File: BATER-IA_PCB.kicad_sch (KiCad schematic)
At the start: 21 parts, among them J1 PJ-202A, J11 Conn_01x08, J15 Conn_01x08, J17 Conn_01x08, J21 Conn_01x10, J23 Conn_01x08, J5 Conn_01x08, J8 Conn_02x18_Counter_Clockwise, U1 74LS245, U17 74LS245, U2 74LS245, U3 74LS245, U4 L7805CV, U5 LD1117V33

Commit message: BUGFIX: The Diagram error in to relay module was fixed.
The routing error in the relay diagram was fixed, also, a prototype of the relay circuit was build and the functionality was validated satisfactorily
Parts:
- removed C1: 100uF, Capacitor_THT:CP_Radial_D8.0mm_P5.00mm, symbol Device:C
- removed C2: 330nF, Capacitor_THT:C_Disc_D8.0mm_W5.0mm_P5.00mm, symbol Device:C
- removed C3, C4: 100nF, Capacitor_THT:C_Disc_D8.0mm_W5.0mm_P5.00mm, symbol Device:C
- removed C5: 10uF, Capacitor_THT:CP_Radial_D8.0mm_P5.00mm, symbol Device:C
- removed D15: 1N5819, digikey-footprints:DO-41, symbol dk_Diodes-Rectifiers-Single:1N5819
- removed F1: 2A, Fuse:Fuseholder_Clip-5x20mm_Bel_FC-203-22_Lateral_P17.80x5.00mm_D1.17mm_Horizontal, symbol Device:Fuse
- removed J1: PJ-202A, digikey-footprints:Barrel_Jack_5.5mmODx2.1mmID_PJ-202A, symbol dk_Barrel-Power-Connectors:PJ-202A
- removed J15, J17, J23, J5: Conn_01x08, Connector_PinHeader_2.54mm:PinHeader_1x08_P2.54mm_Vertical, symbol Connector_Generic:Conn_01x08
- removed J21: Conn_01x10, Connector_PinHeader_2.54mm:PinHeader_1x08_P2.54mm_Vertical, symbol Connector_Generic:Conn_01x10
- removed J8: Conn_02x18_Counter_Clockwise, Connector_PinHeader_2.54mm:PinHeader_2x18_P2.54mm_Vertical, symbol Connector_Generic:Conn_02x18_Counter_Clockwise
- removed U1, U17, U2, U3: 74LS245, Package_DIP:DIP-20_W7.62mm_LongPads, symbol 74xx:74LS245
- removed U4: L7805CV, digikey-footprints:TO-220-3, symbol dk_PMIC-Voltage-Regulators-Linear:L7805CV
- removed U5: LD1117V33, digikey-footprints:TO-220-3, symbol dk_PMIC-Voltage-Regulators-Linear:LD1117V33
- added J1: Conn_01x03, Connector_PinHeader_2.54mm:PinHeader_1x03_P2.54mm_Vertical, symbol Connector_Generic:Conn_01x03
- added J3: Conn_01x12, Connector_PinHeader_2.54mm:PinHeader_1x12_P2.54mm_Vertical, symbol Connector_Generic:Conn_01x12
- added J4: Conn_02x17_Counter_Clockwise, symbol Connector_Generic:Conn_02x17_Counter_Clockwise
- renumbered J11 to J2
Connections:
- net D22: now also J4.1 (Pin_1)
- net D23: now also J4.34 (Pin_34)
- net D24: now also J4.2 (Pin_2)
- net D25: now also J4.33 (Pin_33)
- net D26: now also J4.3 (Pin_3)
- net D27: now also J4.32 (Pin_32)
- net D28: now also J4.4 (Pin_4)
- net D29: now also J4.31 (Pin_31)
- net D30: now also J4.5 (Pin_5)
- net D31: now also J4.30 (Pin_30)
- net D32: now also J4.6 (Pin_6)
- net D33: now also J4.29 (Pin_29)
- net D34: now also J4.7 (Pin_7)
- net D35: now also J4.28 (Pin_28)
- net D36: now also J4.8 (Pin_8)
- net D37: now also J4.27 (Pin_27)
- net D38: now also J4.9 (Pin_9)
- net D39: now also J4.26 (Pin_26)
- net D40: now also J4.10 (Pin_10)
- net D41: now also J4.25 (Pin_25)
- net D42: now also J4.11 (Pin_11)
- net D43: now also J4.24 (Pin_24)
- net D44: now also J4.12 (Pin_12)
- net D45: now also J4.23 (Pin_23)
- net D46: now also J4.13 (Pin_13)
- net D47: now also J4.22 (Pin_22)
- net D48: now also J4.14 (Pin_14)
- net D49: now also J4.21 (Pin_21)
- net D50: now also J4.15 (Pin_15)
- net D51: now also J4.20 (Pin_20)
- net D52: now also J4.16 (Pin_16)
- net D53: now also J4.19 (Pin_19)
- net GND: now also J1.3 (Pin_3), J4.17 (Pin_17), J4.18 (Pin_18)
- net SCL1: now also J1.1 (Pin_1)
- net SDA1: now also J1.2 (Pin_2)
- new net PWM_02: J3.12 (Pin_12)
- new net PWM_03: J3.11 (Pin_11)
- new net PWM_04: J3.10 (Pin_10)
- new net PWM_05: J3.9 (Pin_9)
- new net PWM_06: J3.8 (Pin_8)
- new net PWM_07: J3.7 (Pin_7)
- new net PWM_08: J3.6 (Pin_6)
- new net PWM_09: J3.5 (Pin_5)
- new net PWM_10: J3.4 (Pin_4)
- new net PWM_11: J3.3 (Pin_3)
- new net PWM_12: J3.2 (Pin_2)
- new net PWM_13: J3.1 (Pin_1)
- no-connect marks 27 -> 0
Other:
- sheet RELAY MODULE renamed RELAY MODULE 1
- removed sheet BMS
- added sheet BUFFER LEVEL SHIFTER (Buffer_level_shifters.kicad_sch)
- added sheet RELAY MODULE 2 (RELAY_MODULE_1_REV1.kicad_sch)
- added sheet VOLTAGE REGULATION MODULE (Voltage_regulation_module.kicad_sch)
- sheet RELAY MODULE 1: file RELAY_MODULE_V1.kicad_sch -> RELAY_MODULE_1_REV1.kicad_sch
- sheet RELAY MODULE 1 ports: added K1_COM, K1_N_C, K1_N_O, K2_COM, K2_N_C, K2_N_O, K3_COM, K3_N_C, K3_N_O, K4_COM, K4_N_C, K4_N_O, K5_COM, K5_N_C, K5_N_O, K6_COM, K6_N_C, K6_N_O; removed K10, K11, K7, K8, K9
- note added: "Buffer enable pins"
- moved on the sheet: J2

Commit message: PCB REV 001 design
The design of the first revition of the PCB is complete.
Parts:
- added C1: 100uF, Capacitor_THT:CP_Radial_D8.0mm_P5.00mm, symbol Device:C
- added D1, D11, D13, D15, D17, D3, D5, D7, D9: 1N5817, digikey-footprints:DO-41, symbol dk_Diodes-Rectifiers-Single:1N5819
- added D10, D12, D14, D16, D2, D4, D6, D8: 3.3V, Diode_THT:D_DO-35_SOD27_P10.16mm_Horizontal, symbol Device:D_Zener
- added F1: 2A, Fuse:Fuseholder_Clip-5x20mm_Bel_FC-203-22_Lateral_P17.80x5.00mm_D1.17mm_Horizontal, symbol Device:Fuse
- added J10: PWM CH4, Connector_PinHeader_2.54mm:PinHeader_1x03_P2.54mm_Vertical, symbol Connector_Generic:Conn_01x03
- added J11: PWM CH5, Connector_PinHeader_2.54mm:PinHeader_1x03_P2.54mm_Vertical, symbol Connector_Generic:Conn_01x03
- added J12: PWM CH6, Connector_PinHeader_2.54mm:PinHeader_1x03_P2.54mm_Vertical, symbol Connector_Generic:Conn_01x03
- added J13, J14, J15: PWM GP CH1, Connector_PinHeader_2.54mm:PinHeader_1x03_P2.54mm_Vertical, symbol Connector_Generic:Conn_01x03
- added J16: STP_MOTOR_1, digikey-footprints:PinHeader_1x5_P2.5mm_Drill1.1mm, symbol dk_Rectangular-Connectors-Headers-Male-Pins:B5B-XH-A_LF__SN_
- added J17: STP_MOTOR_2, digikey-footprints:PinHeader_1x5_P2.5mm_Drill1.1mm, symbol dk_Rectangular-Connectors-Headers-Male-Pins:B5B-XH-A_LF__SN_
- added J18: STP_MOTOR_3, digikey-footprints:PinHeader_1x5_P2.5mm_Drill1.1mm, symbol dk_Rectangular-Connectors-Headers-Male-Pins:B5B-XH-A_LF__SN_
- added J19: CELL 1, digikey-footprints:PinHeader_1x2_P2.5mm_Drill1.1mm, symbol dk_Rectangular-Connectors-Headers-Male-Pins:B2B-XH-A_LF__SN_
- added J20: CELL 2, digikey-footprints:PinHeader_1x2_P2.5mm_Drill1.1mm, symbol dk_Rectangular-Connectors-Headers-Male-Pins:B2B-XH-A_LF__SN_
- added J21: CELL 3, digikey-footprints:PinHeader_1x2_P2.5mm_Drill1.1mm, symbol dk_Rectangular-Connectors-Headers-Male-Pins:B2B-XH-A_LF__SN_
- added J22: LIN ACT 1, digikey-footprints:PinHeader_1x2_P2.5mm_Drill1.1mm, symbol dk_Rectangular-Connectors-Headers-Male-Pins:B2B-XH-A_LF__SN_
- added J23: LIN ACT 2, digikey-footprints:PinHeader_1x2_P2.5mm_Drill1.1mm, symbol dk_Rectangular-Connectors-Headers-Male-Pins:B2B-XH-A_LF__SN_
- added J24: LIN ACT 3, digikey-footprints:PinHeader_1x2_P2.5mm_Drill1.1mm, symbol dk_Rectangular-Connectors-Headers-Male-Pins:B2B-XH-A_LF__SN_
- added J5: GPIOS, Connector_PinHeader_2.54mm:PinHeader_1x08_P2.54mm_Vertical, symbol Connector_Generic:Conn_01x08
- added J6: PJ-202A, digikey-footprints:Barrel_Jack_5.5mmODx2.1mmID_PJ-202A, symbol dk_Barrel-Power-Connectors:PJ-202A
- added J7: PWM CH1, Connector_PinHeader_2.54mm:PinHeader_1x03_P2.54mm_Vertical, symbol Connector_Generic:Conn_01x03
- added J8: PWM CH2, Connector_PinHeader_2.54mm:PinHeader_1x03_P2.54mm_Vertical, symbol Connector_Generic:Conn_01x03
- added J9: PWM CH3, Connector_PinHeader_2.54mm:PinHeader_1x03_P2.54mm_Vertical, symbol Connector_Generic:Conn_01x03
- added R1, R2, R3: 5.1, Resistor_THT:R_Axial_DIN0614_L14.3mm_D5.7mm_P15.24mm_Horizontal, symbol Device:R_US
- J2: renamed from J1; value Conn_01x03 -> MCU_I2C_1
- J3: value Conn_01x12 -> MCU_PWM_INPUT
- J4: value Conn_02x17_Counter_Clockwise -> MCU_GPIOS_NPUT; footprint (none) -> Connector_PinHeader_2.54mm:PinHeader_2x17_P2.54mm_Vertical
- renumbered J2 to J1
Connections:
- net +3.3V: now also D1.K, D11.K, D13.K, D15.K, D3.K, D5.K, D7.K, D9.K
- net +5V: now also J10.1 (Pin_1), J11.1 (Pin_1), J12.1 (Pin_1), J13.1 (Pin_1), J14.1 (Pin_1), J15.1 (Pin_1), J7.1 (Pin_1), J8.1 (Pin_1), J9.1 (Pin_1)
- net ADC_CH0: now also D1.A, D2.1 (K)
- net ADC_CH1: now also D3.A, D4.1 (K)
- net ADC_CH2: now also D5.A, D6.1 (K)
- net ADC_CH3: now also D7.A, D8.1 (K)
- net ADC_CH4: now also D10.1 (K), D9.A
- net ADC_CH5: now also D11.A, D12.1 (K)
- net ADC_CH6: now also D13.A, D14.1 (K)
- net ADC_CH7: now also D15.A, D16.1 (K)
- net BUFFER LEVEL SHIFTER/GPIO_D43_5V: now also J5.2 (Pin_2)
- net BUFFER LEVEL SHIFTER/GPIO_D44_5V: now also J5.4 (Pin_4)
- net BUFFER LEVEL SHIFTER/GPIO_D45_5V: now also J5.3 (Pin_3)
- net BUFFER LEVEL SHIFTER/GPIO_D46_5V: now also J5.5 (Pin_5)
- net BUFFER LEVEL SHIFTER/GPIO_D47_5V: now also J5.6 (Pin_6)
- net BUFFER LEVEL SHIFTER/GPIO_D48_5V: now also J5.7 (Pin_7)
- net GND: now also C1.2, D10.2 (A), D12.2 (A), D14.2 (A), D16.2 (A), D2.2 (A), D4.2 (A), D6.2 (A), D8.2 (A), J10.3 (Pin_3), J11.3 (Pin_3), J12.3 (Pin_3), J13.3 (Pin_3), J14.3 (Pin_3), J15.3 (Pin_3), J19.2, J20.2, J21.2, J22.2, J23.2, J24.2, J5.1 (Pin_1), J5.8 (Pin_8), J6.2, J6.3, J7.3 (Pin_3), J8.3 (Pin_3), J9.3 (Pin_3), R1.2, R2.2, R3.2
- new net: C1.1, D17.K, F1.1
- new net: D17.A, J6.1
- new net +12V: F1.2
- new net CELL_1: J19.1
- new net CELL_2: J20.1
- new net CELL_3: J21.1
- new net LINEAR_ACT_1: J22.1
- new net LINEAR_ACT_2: J23.1
- new net LINEAR_ACT_3: J24.1
- new net PWM_5V_GP_1: J13.2 (Pin_2)
- new net PWM_5V_GP_2: J14.2 (Pin_2)
- new net PWM_5V_GP_3: J15.2 (Pin_2)
- new net PWM_SERVO_1: J7.2 (Pin_2)
- new net PWM_SERVO_2: J8.2 (Pin_2)
- new net PWM_SERVO_3: J9.2 (Pin_2)
- new net PWM_SERVO_4: J10.2 (Pin_2)
- new net PWM_SERVO_5: J11.2 (Pin_2)
- new net PWM_SERVO_6: J12.2 (Pin_2)
- new net RELAY MODULE 1/K4_N_O: R1.1
- new net RELAY MODULE 1/K5_N_O: R2.1
- new net RELAY MODULE 1/K6_N_C: R3.1
- new net STEPPER MOTOR DRIVER/STP_M1_OUT_1: J16.2
- new net STEPPER MOTOR DRIVER/STP_M1_OUT_2: J16.3
- new net STEPPER MOTOR DRIVER/STP_M1_OUT_3: J16.4
- new net STEPPER MOTOR DRIVER/STP_M1_OUT_4: J16.5
- new net STEPPER MOTOR DRIVER/STP_M1_OUT_COM: J16.1
- new net STEPPER MOTOR DRIVER/STP_M2_OUT_1: J17.2
- new net STEPPER MOTOR DRIVER/STP_M2_OUT_2: J17.3
- new net STEPPER MOTOR DRIVER/STP_M2_OUT_3: J17.4
- new net STEPPER MOTOR DRIVER/STP_M2_OUT_4: J17.5
- new net STEPPER MOTOR DRIVER/STP_M2_OUT_COM: J17.1
- new net STEPPER MOTOR DRIVER/STP_M3_OUT_1: J18.2
- new net STEPPER MOTOR DRIVER/STP_M3_OUT_2: J18.3
- new net STEPPER MOTOR DRIVER/STP_M3_OUT_3: J18.4
- new net STEPPER MOTOR DRIVER/STP_M3_OUT_4: J18.5
- new net STEPPER MOTOR DRIVER/STP_M3_OUT_COM: J18.1
- no-connect marks 0 -> 3
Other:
- removed sheet RELAY MODULE 2
- added sheet P BMS (P_BMS.kicad_sch)
- added sheet STEPPER MOTOR DRIVER (StepperMotorDriver.kicad_sch)
- sheet RELAY MODULE 1 ports: added K7, K7_COM, K7_N_C, K7_N_O, K8, K8_COM, K8_N_C, K8_N_O, K9, K9_COM, K9_N_C, K9_N_O; removed none
- sheet VOLTAGE REGULATION MODULE ports: added 12VDC; removed none
- note added: "Clamping protection"
- note added: "Over voltage protection"
- moved on the sheet: J1, J2, J3, J4

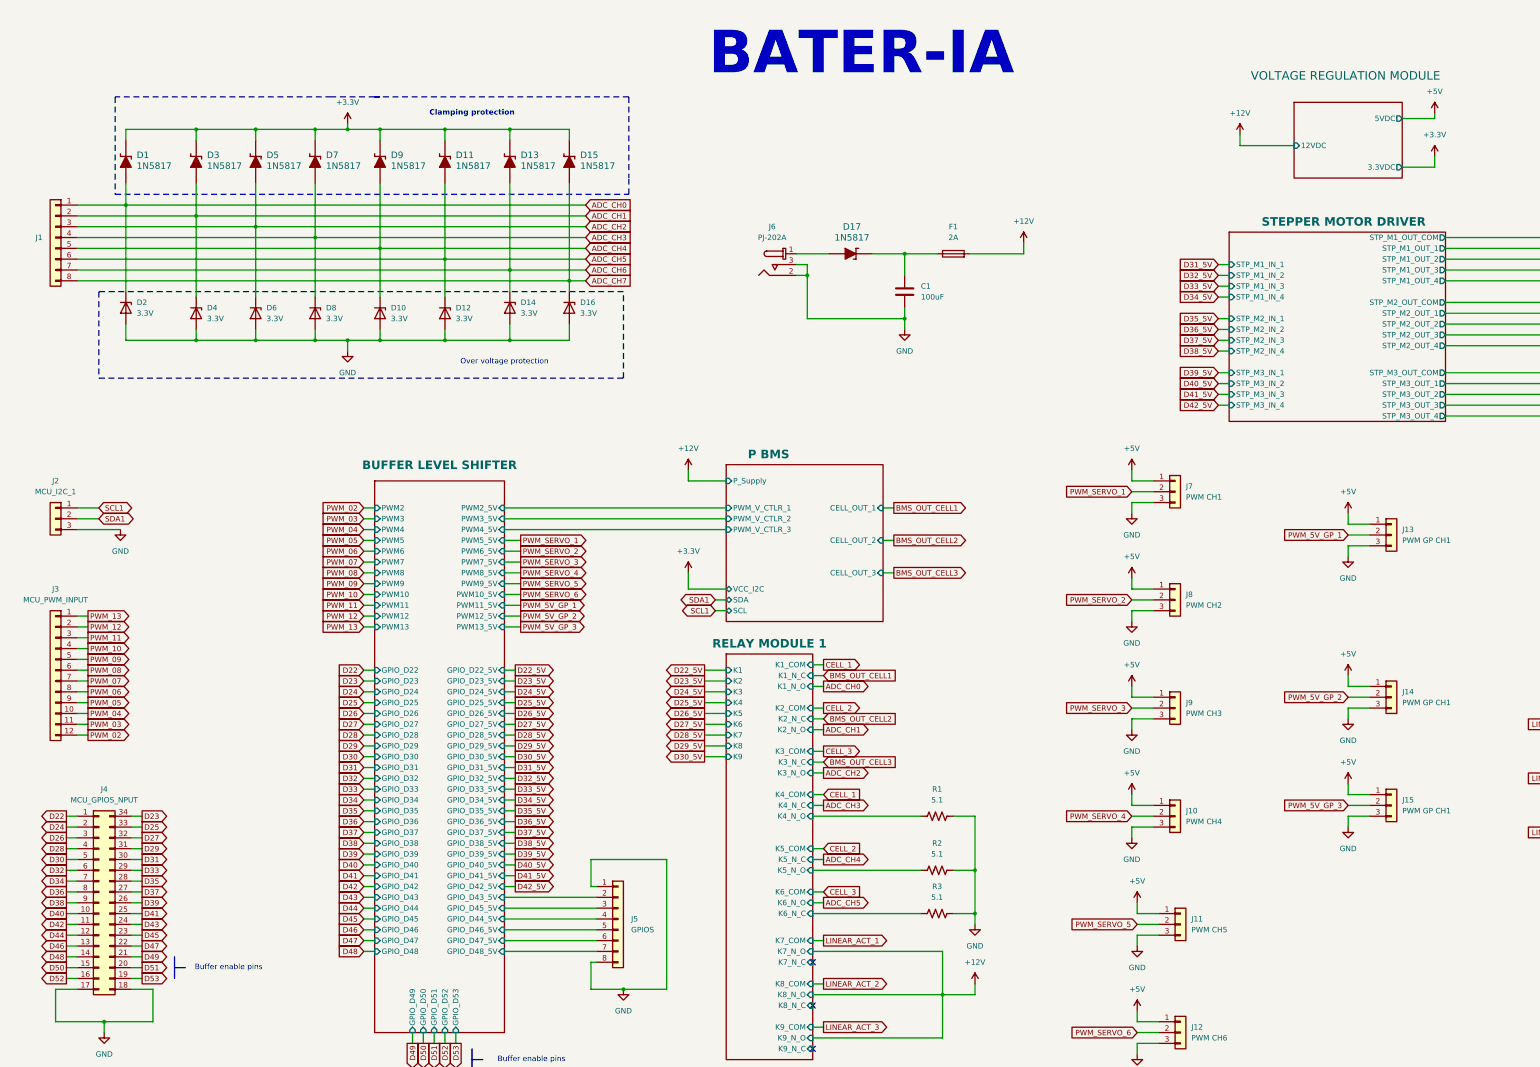
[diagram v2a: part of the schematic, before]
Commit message: PCB 90% & Corrections to diagram in the ADC section were done
Te resistors to secure a low logical level were placed, also the routing of the PCB is at the 90%
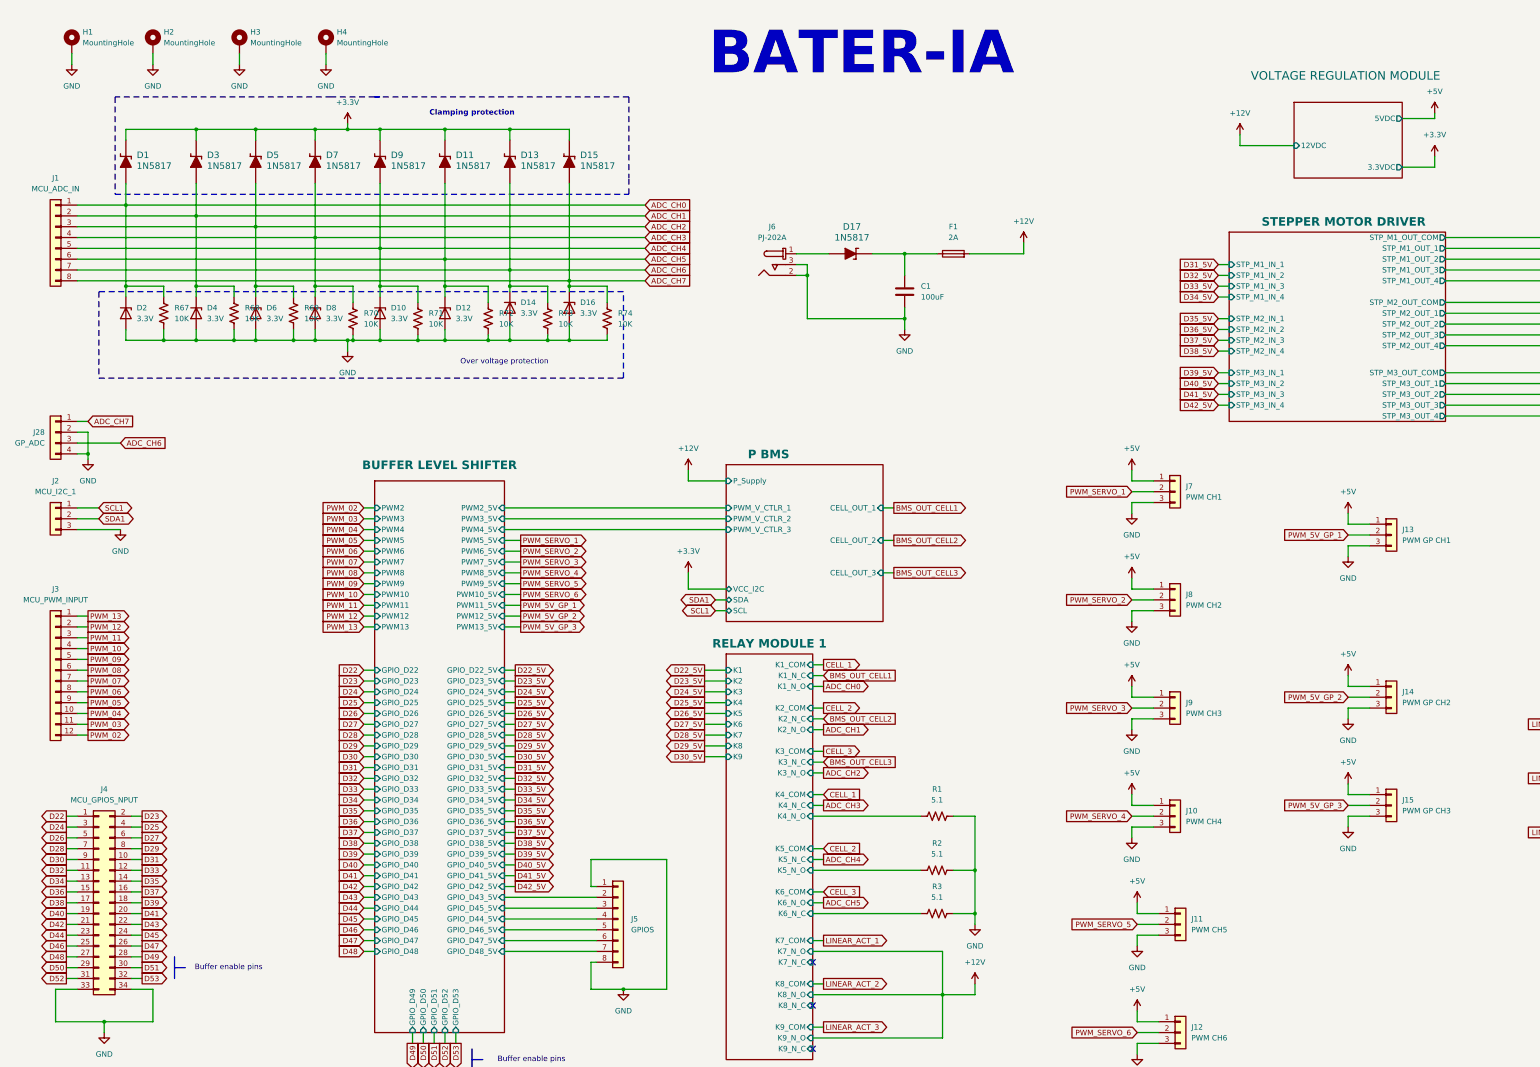
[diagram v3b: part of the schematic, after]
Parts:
- removed J4: MCU_GPIOS_NPUT, Connector_PinHeader_2.54mm:PinHeader_2x17_P2.54mm_Vertical, symbol Connector_Generic:Conn_02x17_Counter_Clockwise
- added H1, H2, H3, H4: MountingHole, MountingHole:MountingHole_2.2mm_M2_DIN965_Pad_TopBottom, symbol Mechanical:MountingHole_Pad
- added J28: GP_ADC, Connector_PinHeader_2.54mm:PinHeader_1x04_P2.54mm_Vertical, symbol Connector_Generic:Conn_01x04
- added J4: MCU_GPIOS_NPUT, Connector_PinHeader_2.54mm:PinHeader_2x17_P2.54mm_Vertical, symbol Connector_Generic:Conn_02x17_Odd_Even
- added R67, R68, R69, R70, R71, R72, R73, R74: 10K, Resistor_THT:R_Axial_DIN0207_L6.3mm_D2.5mm_P7.62mm_Horizontal, symbol Device:R_US
- D1, D11, D13, D15, D17, D3, D5, D7, D9: footprint digikey-footprints:DO-41 -> Myfoodprints:D_DO-41_SOD81_P9.20mm_Horizontal
- J1: value Conn_01x08 -> MCU_ADC_IN
- J14: value PWM GP CH1 -> PWM GP CH2
- J15: value PWM GP CH1 -> PWM GP CH3
- J6: footprint digikey-footprints:Barrel_Jack_5.5mmODx2.1mmID_PJ-202A -> Connector_BarrelJack:BarrelJack_Horizontal
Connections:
- net ADC_CH0: now also R67.1
- net ADC_CH1: now also R68.1
- net ADC_CH2: now also R69.1
- net ADC_CH3: now also R70.1
- net ADC_CH4: now also R71.1
- net ADC_CH5: now also R72.1
- net ADC_CH6: now also J28.3 (Pin_3), R73.1
- net ADC_CH7: now also J28.1 (Pin_1), R74.1
- net D22: now also J4.1 (Pin_1)
- net D23: now also J4.2 (Pin_2)
- net D24: now also J4.3 (Pin_3)
- net D25: now also J4.4 (Pin_4)
- net D26: now also J4.5 (Pin_5)
- net D27: now also J4.6 (Pin_6)
- net D28: now also J4.7 (Pin_7)
- net D29: now also J4.8 (Pin_8)
- net D30: now also J4.9 (Pin_9)
- net D31: now also J4.10 (Pin_10)
- net D32: now also J4.11 (Pin_11)
- net D33: now also J4.12 (Pin_12)
- net D34: now also J4.13 (Pin_13)
- net D35: now also J4.14 (Pin_14)
- net D36: now also J4.15 (Pin_15)
- net D37: now also J4.16 (Pin_16)
- net D38: now also J4.17 (Pin_17)
- net D39: now also J4.18 (Pin_18)
- net D40: now also J4.19 (Pin_19)
- net D41: now also J4.20 (Pin_20)
- net D42: now also J4.21 (Pin_21)
- net D43: now also J4.22 (Pin_22)
- net D44: now also J4.23 (Pin_23)
- net D45: now also J4.24 (Pin_24)
- net D46: now also J4.25 (Pin_25)
- net D47: now also J4.26 (Pin_26)
- net D48: now also J4.27 (Pin_27)
- net D49: now also J4.28 (Pin_28)
- net D50: now also J4.29 (Pin_29)
- net D51: now also J4.30 (Pin_30)
- net D52: now also J4.31 (Pin_31)
- net D53: now also J4.32 (Pin_32)
- net GND: now also H1.1, H2.1, H3.1, H4.1, J28.2 (Pin_2), J28.4 (Pin_4), J4.33 (Pin_33), J4.34 (Pin_34), R67.2, R68.2, R69.2, R70.2, R71.2, R72.2, R73.2, R74.2
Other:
- moved on the sheet: D2
